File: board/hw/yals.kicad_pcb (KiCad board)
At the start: 2 copper layers, 37 parts, among them J1 SWD, J2 UART, J3 eng, U1 RP2040, U2 M24C02-FMN, U3 MCP1703Ax-330xxTT, U4 W25Q32JVSS, U5 DRV8220, U6 LM321, Y1 Crystal

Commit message: PCB elements positioning - WIP
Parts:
- moved J2 34.5 mm to (188.0, 73.7)
- moved U5 29.2 mm to (182.1, 84.3)
- moved U1 13.3 mm to (157.5, 85.5)
- moved R6 8.35 mm to (181.6, 90.2), turned to -90 degrees
- moved J3 4.11 mm to (188.0, 86.4)
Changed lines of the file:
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@@
   )
   (footprint "Resistor_SMD:R_1206_3216Metric" (layer "F.Cu")
-    (at 189.0375 86.36)
+    (at 181.61 90.17 -90)
     (descr "Resistor SMD 1206 (3216 Metric), square (rectangular) end terminal, IPC_7351 nominal, (Body size source: IPC-SM-782 page 72, https://www.pcb-3d.com/wordpress/wp-content/uploads/ipc-sm-782a_amendment_1_and_2.pdf), generated with kicad-footprint-generator")
     (tags "resistor")
@@
     (property "ki_keywords" "R res resistor")
     (attr smd)
-    (fp_text reference "R6" (at 0 -1.82) (layer "F.SilkS")
-        (effects (font (size 1 1) (thickness 0.15)))
-    )
-    (fp_text value "0.1R" (at 0 1.82) (layer "F.Fab")
-        (effects (font (size 1 1) (thickness 0.15)))
-    )
-    (fp_text user "${REFERENCE}" (at 0 0) (layer "F.Fab")
+    (fp_text reference "R6" (at 0 -1.82 90) (layer "F.SilkS")
+        (effects (font (size 1 1) (thickness 0.15)))
+    )
+    (fp_text value "0.1R" (at 0 1.82 90) (layer "F.Fab")
+        (effects (font (size 1 1) (thickness 0.15)))
+    )
+    (fp_text user "${REFERENCE}" (at 0 0 90) (layer "F.Fab")
         (effects (font (size 0.8 0.8) (thickness 0.12)))
     )
@@
     (fp_line (start 1.6 0.8) (end -1.6 0.8)
       (stroke (width 0.1) (type solid)) (layer "F.Fab"))
-    (pad "1" smd roundrect (at -1.4625 0) (size 1.125 1.75) (layers "F.Cu" "F.Paste" "F.Mask") (roundrect_rratio 0.222222)
+    (pad "1" smd roundrect (at -1.4625 0 270) (size 1.125 1.75) (layers "F.Cu" "F.Paste" "F.Mask") (roundrect_rratio 0.222222)
       (net 52 "Net-(U5-GND)") (pintype "passive"))
-    (pad "2" smd roundrect (at 1.4625 0) (size 1.125 1.75) (layers "F.Cu" "F.Paste" "F.Mask") (roundrect_rratio 0.222222)
+    (pad "2" smd roundrect (at 1.4625 0 270) (size 1.125 1.75) (layers "F.Cu" "F.Paste" "F.Mask") (roundrect_rratio 0.222222)
       (net 35 "GND") (pintype "passive"))
     (model "${KICAD6_3DMODEL_DIR}/Resistor_SMD.3dshapes/R_1206_3216Metric.wrl"
@@
   )
   (footprint "Package_TO_SOT_SMD:SOT-563" (layer "F.Cu")
-    (at 154.19 75.7)
+    (at 182.13 84.32)
     (descr "SOT563")
     (tags "SOT-563")
@@
   )
   (footprint "Connector_PinHeader_2.54mm:PinHeader_1x03_P2.54mm_Vertical" (layer "F.Cu")
-    (at 154.94 83.82)
+    (at 187.96 73.66)
     (descr "Through hole straight pin header, 1x03, 2.54mm pitch, single row")
     (tags "Through hole pin header THT 1x03 2.54mm single row")
@@
   )
   (footprint "Package_DFN_QFN:QFN-56-1EP_7x7mm_P0.4mm_EP3.2x3.2mm" (layer "F.Cu")
-    (at 163.4575 73.6)
+    (at 157.54 85.4625)
     (descr "QFN, 56 Pin (https://datasheets.raspberrypi.com/rp2040/rp2040-datasheet.pdf#page=634), generated with kicad-footprint-generator ipc_noLead_generator.py")
     (tags "QFN NoLead")
@@
   )
   (footprint "Connector_PinHeader_2.54mm:PinHeader_1x02_P2.54mm_Vertical" (layer "F.Cu")
-    (at 183.9075 87.04)
+    (at 187.96 86.36)
     (descr "Through hole straight pin header, 1x02, 2.54mm pitch, single row")
     (tags "Through hole pin header THT 1x02 2.54mm single row")

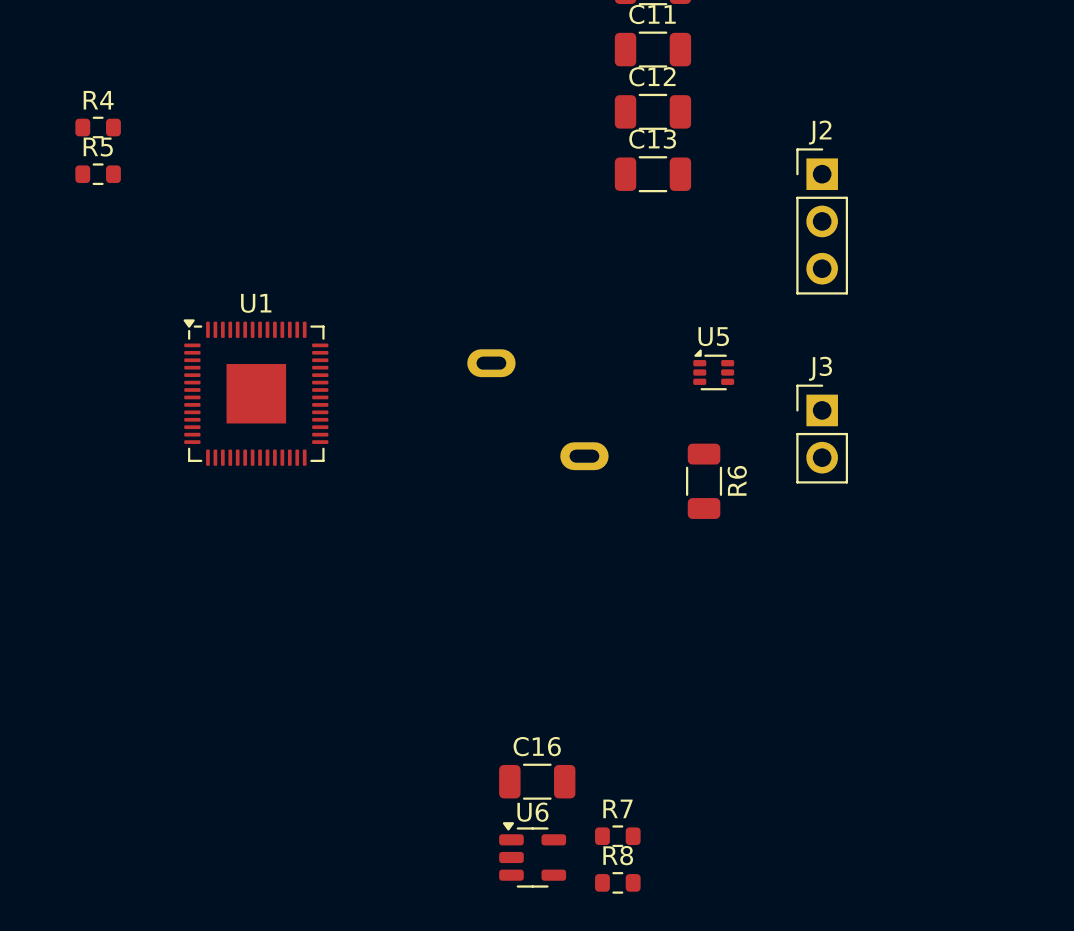
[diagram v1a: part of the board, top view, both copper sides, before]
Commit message: engine ctrl and feedback loop elements placed
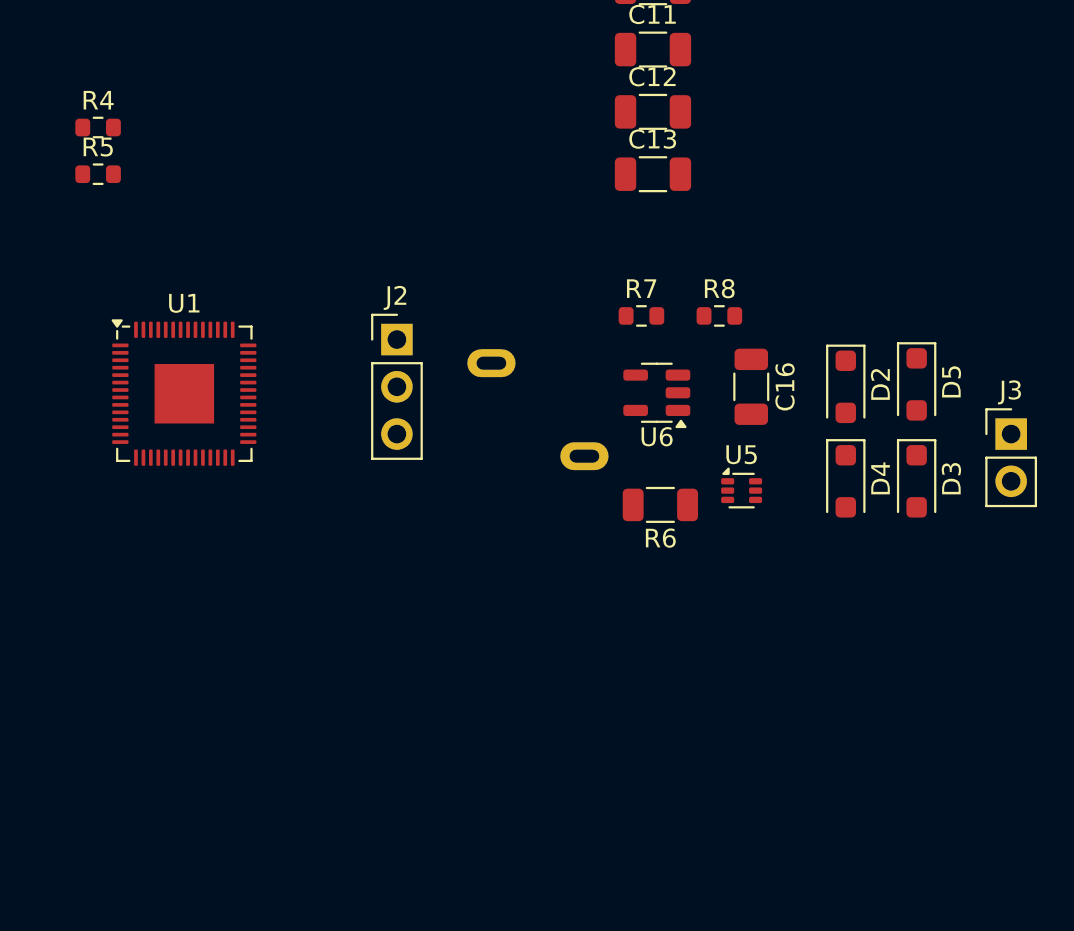
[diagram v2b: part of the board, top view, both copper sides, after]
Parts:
- added D2: 1N4007, Diode_SMD:D_SOD-123F, F.Cu at (189.2, 85.1)
- added D3: 1N4007, Diode_SMD:D_SOD-123F, F.Cu at (193.0, 90.2)
- added D4: 1N4007, Diode_SMD:D_SOD-123F, F.Cu at (189.2, 90.2)
- added D5: 1N4007, Diode_SMD:D_SOD-123F, F.Cu at (193.0, 85.0)
- moved R8 31.0 mm to (182.4, 81.3)
- moved R7 28.0 mm to (178.2, 81.3)
- moved U6 25.9 mm to (179.1, 85.4), turned to 180 degrees
- moved J2 24.5 mm to (165.1, 82.5)
- moved C16 24.1 mm to (184.2, 85.1), turned to -90 degrees
- moved J3 10.2 mm to (198.1, 87.6)
- moved U5 6.52 mm to (183.6, 90.7)
- moved U1 3.87 mm to (153.7, 85.5)
- moved R6 2.67 mm to (179.3, 91.4), turned to 180 degrees

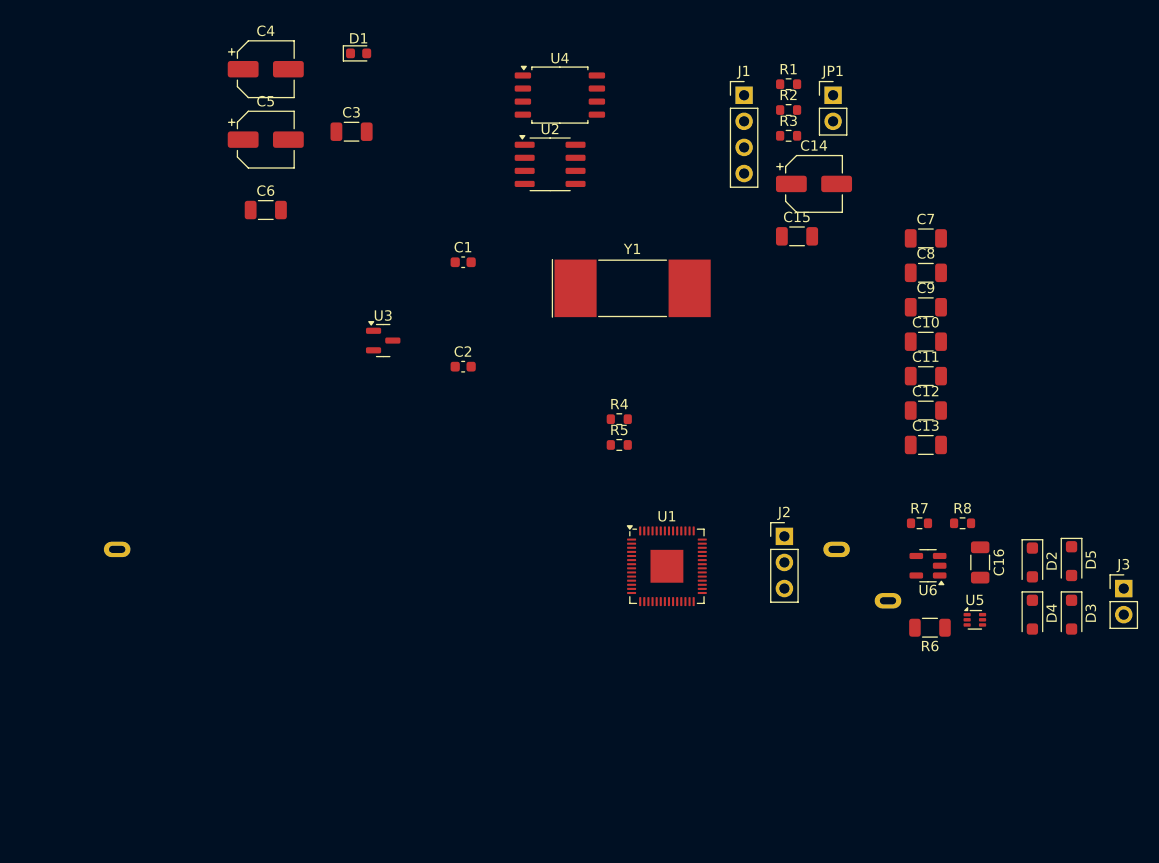
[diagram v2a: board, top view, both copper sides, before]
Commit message: added board's outer dimensions, placed some more components and added missing power supply slot
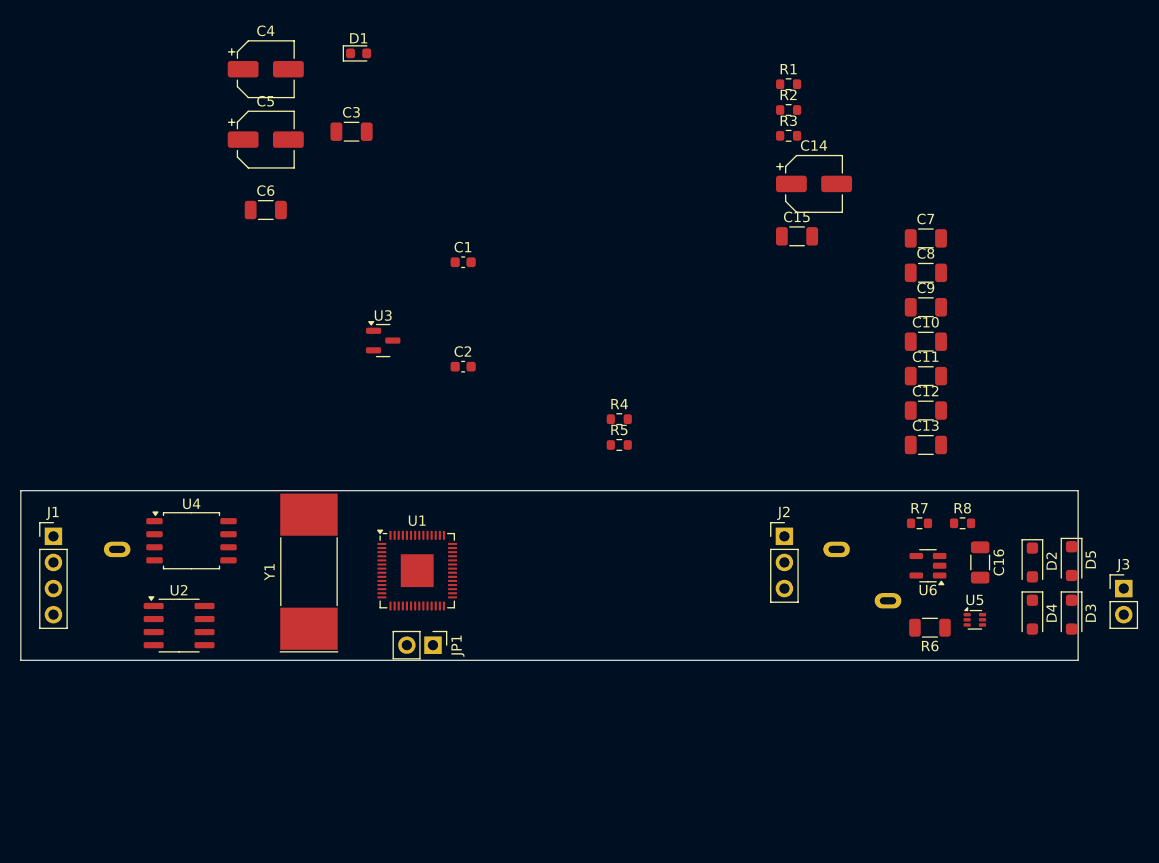
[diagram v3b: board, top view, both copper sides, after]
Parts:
- moved J1 79.7 mm to (94.0, 82.5)
- moved JP1 66.2 mm to (130.9, 93.1), turned to -90 degrees
- moved U2 57.6 mm to (106.2, 91.2)
- moved U4 56.3 mm to (107.4, 83.0)
- moved Y1 41.9 mm to (118.8, 86.0), turned to 90 degrees
- moved U1 24.3 mm to (129.4, 85.9)
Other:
- board outline added: 102.9 x 16.5 mm
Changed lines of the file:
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@@
   )
   (footprint "Package_SO:SOIC-8_3.9x4.9mm_P1.27mm" (layer "F.Cu")
-    (at 142.305 46.355)
+    (at 106.2075 91.2325)
     (descr "SOIC, 8 Pin (JEDEC MS-012AA, https://www.analog.com/media/en/package-pcb-resources/package/pkg_pdf/soic_narrow-r/r_8.pdf), generated with kicad-footprint-generator ipc_gullwing_generator.py")
     (tags "SOIC SO")
@@
   )
   (footprint "Connector_PinHeader_2.54mm:PinHeader_1x02_P2.54mm_Vertical" (layer "F.Cu")
-    (at 169.84 39.63)
+    (at 130.9075 93.1375 -90)
     (descr "Through hole straight pin header, 1x02, 2.54mm pitch, single row")
     (tags "Through hole pin header THT 1x02 2.54mm single row")
@@
     (property "ki_keywords" "Jumper SPST")
     (attr through_hole)
-    (fp_text reference "JP1" (at 0 -2.33) (layer "F.SilkS")
-        (effects (font (size 1 1) (thickness 0.15)))
-    )
-    (fp_text value "BOOTSEL" (at 0 4.87) (layer "F.Fab")
-        (effects (font (size 1 1) (thickness 0.15)))
-    )
-    (fp_text user "${REFERENCE}" (at 0 1.27 90) (layer "F.Fab")
+    (fp_text reference "JP1" (at 0 -2.33 90) (layer "F.SilkS")
+        (effects (font (size 1 1) (thickness 0.15)))
+    )
+    (fp_text value "BOOTSEL" (at 0 4.87 90) (layer "F.Fab")
+        (effects (font (size 1 1) (thickness 0.15)))
+    )
+    (fp_text user "${REFERENCE}" (at 0 1.27) (layer "F.Fab")
         (effects (font (size 1 1) (thickness 0.15)))
     )
@@
     (fp_line (start 1.27 3.81) (end -1.27 3.81)
       (stroke (width 0.1) (type solid)) (layer "F.Fab"))
-    (pad "1" thru_hole rect (at 0 0) (size 1.7 1.7) (drill 1) (layers "*.Cu" "*.Mask")
+    (pad "1" thru_hole rect (at 0 0 270) (size 1.7 1.7) (drill 1) (layers "*.Cu" "*.Mask")
       (net 44 "Net-(JP1-A)") (pinfunction "A") (pintype "passive"))
-    (pad "2" thru_hole oval (at 0 2.54) (size 1.7 1.7) (drill 1) (layers "*.Cu" "*.Mask")
+    (pad "2" thru_hole oval (at 0 2.54 270) (size 1.7 1.7) (drill 1) (layers "*.Cu" "*.Mask")
       (net 35 "GND") (pinfunction "B") (pintype "passive"))
     (model "${KICAD6_3DMODEL_DIR}/Connector_PinHeader_2.54mm.3dshapes/PinHeader_1x02_P2.54mm_Vertical.wrl"
@@
   )
   (footprint "Connector_PinHeader_2.54mm:PinHeader_1x04_P2.54mm_Vertical" (layer "F.Cu")
-    (at 161.18 39.63)
+    (at 93.98 82.55)
     (descr "Through hole straight pin header, 1x04, 2.54mm pitch, single row")
     (tags "Through hole pin header THT 1x04 2.54mm single row")
@@
   )
   (footprint "Package_SO:SOIC-8_5.23x5.23mm_P1.27mm" (layer "F.Cu")
-    (at 143.255 39.615)
+    (at 107.4125 82.9775)
     (descr "SOIC, 8 Pin (http://www.winbond.com/resource-files/w25q32jv%20revg%2003272018%20plus.pdf#page=68), generated with kicad-footprint-generator ipc_gullwing_generator.py")
     (tags "SOIC SO")
@@
   )
   (footprint "Crystal:Crystal_SMD_SeikoEpson_MA505-2Pin_12.7x5.1mm" (layer "F.Cu")
-    (at 150.33 58.42)
+    (at 118.8425 85.9875 90)
     (descr "SMD Crystal Seiko Epson MC-505 http://media.digikey.com/pdf/Data%20Sheets/Epson%20PDFs/MA-505,506.pdf, 12.7x5.1mm^2 package")
     (tags "SMD SMT crystal")
@@
     (property "ki_keywords" "quartz ceramic resonator oscillator")
     (attr smd)
-    (fp_text reference "Y1" (at 0 -3.8) (layer "F.SilkS")
-        (effects (font (size 1 1) (thickness 0.15)))
-    )
-    (fp_text value "Crystal" (at 0 3.8) (layer "F.Fab")
-        (effects (font (size 1 1) (thickness 0.15)))
-    )
-    (fp_text user "${REFERENCE}" (at 0 0) (layer "F.Fab")
+    (fp_text reference "Y1" (at 0 -3.8 90) (layer "F.SilkS")
+        (effects (font (size 1 1) (thickness 0.15)))
+    )
+    (fp_text value "Crystal" (at 0 3.8 90) (layer "F.Fab")
+        (effects (font (size 1 1) (thickness 0.15)))
+    )
+    (fp_text user "${REFERENCE}" (at 0 0 90) (layer "F.Fab")
         (effects (font (size 1 1) (thickness 0.15)))
     )
@@
     (fp_line (start 6.35 2.54) (end 6.35 -2.54)
       (stroke (width 0.1) (type solid)) (layer "F.Fab"))
-    (pad "1" smd rect (at -5.55 0) (size 4.1 5.6) (layers "F.Cu" "F.Paste" "F.Mask")
+    (pad "1" smd rect (at -5.55 0 90) (size 4.1 5.6) (layers "F.Cu" "F.Paste" "F.Mask")
       (net 37 "Net-(U1-XOUT)") (pinfunction "1") (pintype "passive"))
-    (pad "2" smd rect (at 5.55 0) (size 4.1 5.6) (layers "F.Cu" "F.Paste" "F.Mask")
+    (pad "2" smd rect (at 5.55 0 90) (size 4.1 5.6) (layers "F.Cu" "F.Paste" "F.Mask")
       (net 38 "Net-(U1-XIN)") (pinfunction "2") (pintype "passive"))
     (model "${KICAD6_3DMODEL_DIR}/Crystal.3dshapes/Crystal_SMD_SeikoEpson_MA505-2Pin_12.7x5.1mm.wrl"
@@
   )
   (footprint "Package_DFN_QFN:QFN-56-1EP_7x7mm_P0.4mm_EP3.2x3.2mm" (layer "F.Cu")
-    (at 153.67 85.4625)
+    (at 129.375 85.89)
     (descr "QFN, 56 Pin (https://datasheets.raspberrypi.com/rp2040/rp2040-datasheet.pdf#page=634), generated with kicad-footprint-generator ipc_noLead_generator.py")
     (tags "QFN NoLead")
@@
     (property "ki_keywords" "resistor variable")
     (attr through_hole)
-    (fp_text reference "RV1" (at 0 7.62 unlocked) (layer "B.SilkS")
+    (fp_text reference "RV1" (at 3.0775 7.1925 unlocked) (layer "B.SilkS")
         (effects (font (size 1 1) (thickness 0.1)) (justify mirror))
     )
@@
         (effects (font (size 1 1) (thickness 0.15)) (justify mirror))
     )
-    (fp_text user "${REFERENCE}" (at 0 -7.62 unlocked) (layer "B.Fab")
+    (fp_text user "${REFERENCE}" (at 3.0775 -8.0475 unlocked) (layer "B.Fab")
         (effects (font (size 1 1) (thickness 0.15)) (justify mirror))
     )
@@
       (net 35 "GND") (pinfunction "3") (pintype "passive") (clearance 0.5))
   )
+  (gr_line (start 193.675 78.105) (end 90.805 78.105)
+    (stroke (width 0.05) (type default)) (layer "Edge.Cuts"))
+  (gr_line (start 193.675 94.615) (end 193.675 78.105)
+    (stroke (width 0.05) (type default)) (layer "Edge.Cuts"))
+  (gr_line (start 90.805 78.105) (end 90.805 94.615)
+    (stroke (width 0.05) (type default)) (layer "Edge.Cuts"))
+  (gr_line (start 90.805 94.615) (end 193.675 94.615)
+    (stroke (width 0.05) (type default)) (layer "Edge.Cuts"))
 )

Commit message: initial placement of all components
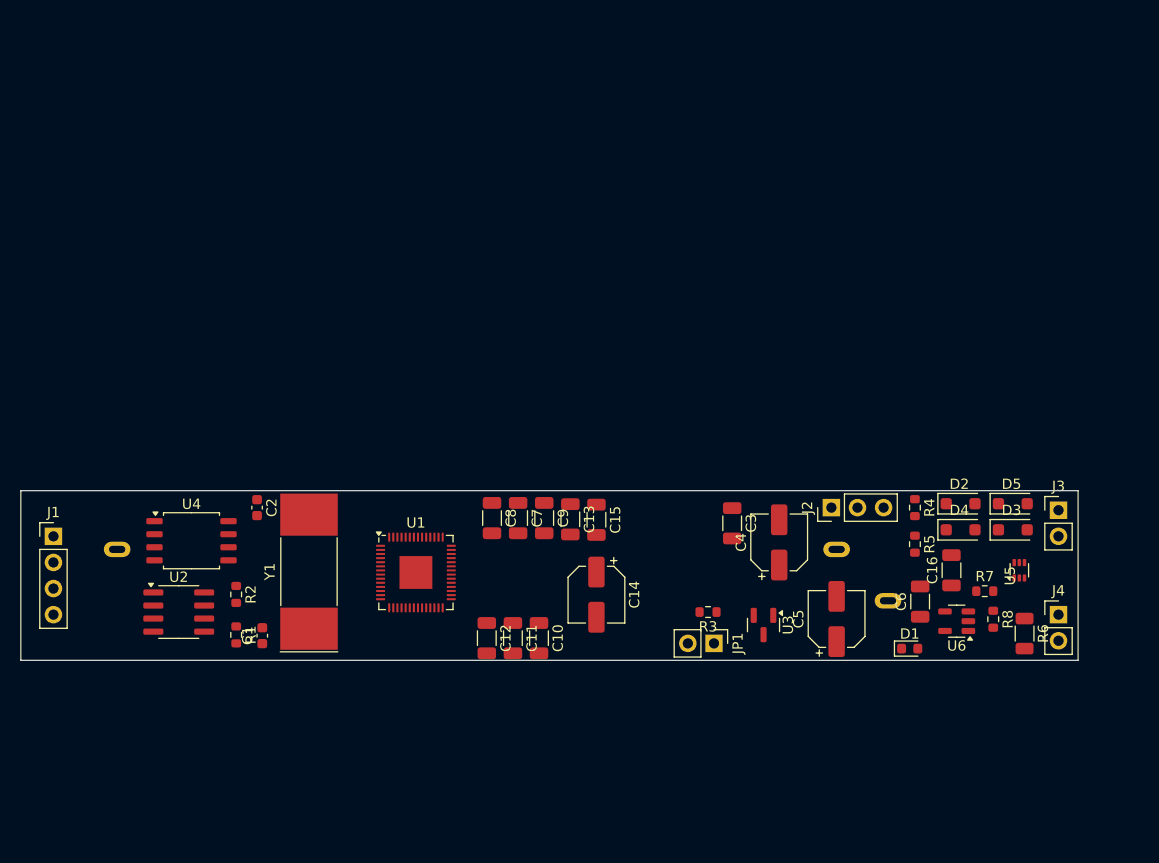
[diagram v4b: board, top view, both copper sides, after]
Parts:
- added J4: power, Connector_PinHeader_2.54mm:PinHeader_1x02_P2.54mm_Vertical, F.Cu at (191.8, 90.2)
- moved D1 78.9 mm to (177.3, 93.5)
- moved R1 75.9 mm to (111.8, 92.1), turned to -90 degrees
- moved C6 74.2 mm to (178.3, 88.9), turned to 90 degrees
- moved C5 72.5 mm to (170.2, 90.6), turned to 90 degrees
- moved R2 71.5 mm to (111.8, 88.2), turned to -90 degrees
- moved C4 67.9 mm to (164.6, 83.1), turned to 90 degrees
- moved C3 53.1 mm to (160.0, 81.3), turned to -90 degrees
- moved C8 48.5 mm to (136.7, 80.8), turned to -90 degrees
- moved C12 48.1 mm to (136.1, 92.5), turned to -90 degrees
- moved C7 48.1 mm to (139.2, 80.8), turned to -90 degrees
- moved C11 47.6 mm to (138.7, 92.5), turned to -90 degrees
- moved C10 47.4 mm to (141.2, 92.5), turned to -90 degrees
- moved R3 47.0 mm to (157.7, 89.9), turned to 180 degrees
- moved U3 46.2 mm to (163.1, 91.2), turned to -90 degrees
- moved C14 45.2 mm to (146.8, 88.2), turned to -90 degrees
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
